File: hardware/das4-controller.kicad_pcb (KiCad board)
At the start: 4 copper layers, 51.1 x 94 mm, 76 parts, among them J1 USB-C, J2 USB-A 1, J3 USB-A 2, J4 Key matrix, SW1 Button 1, SW2 Button 2, SW3 Button 3, SW4 Button 4, SW5 Button 5, SW6 BOOTSEL, SW7 RESET, U1 RP2350B, U2 CH334R, U3 W25Q128JVS, U4 AMS1117-3.3, Y1 12MHz, Y2 12MHz

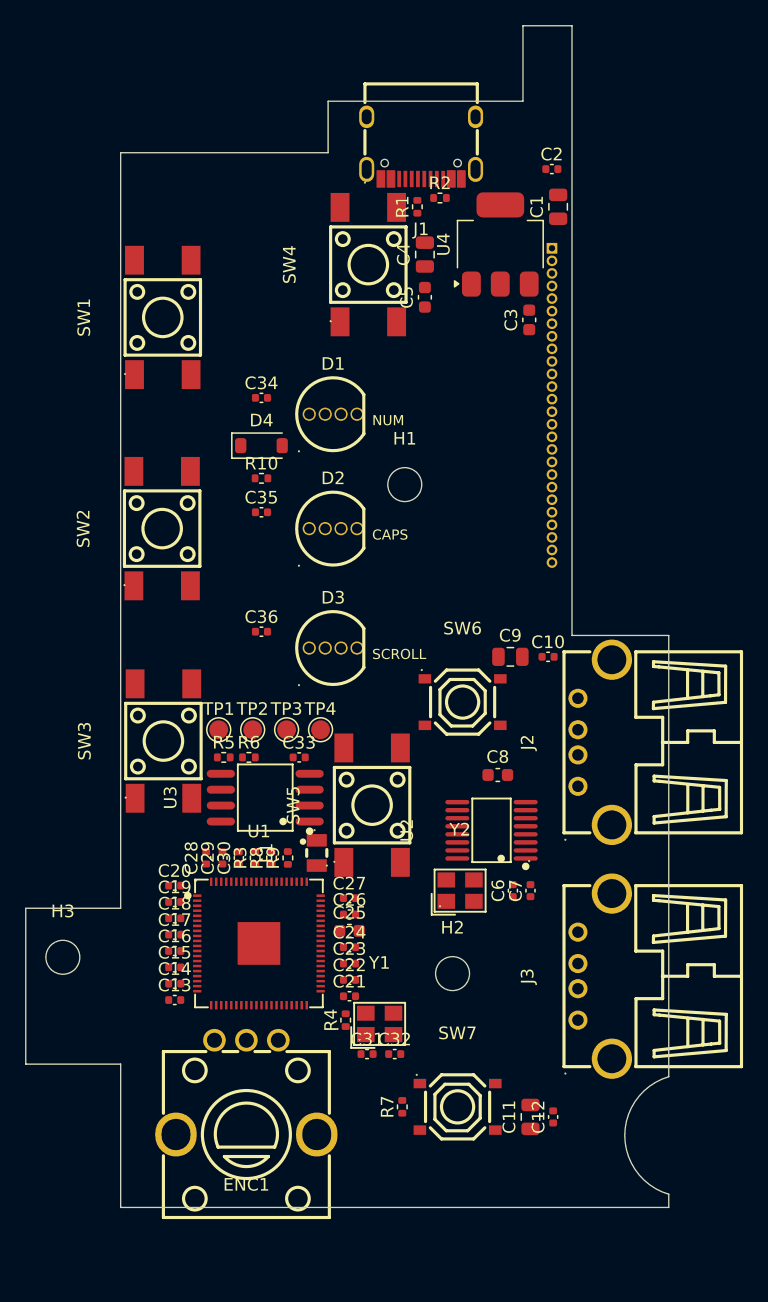
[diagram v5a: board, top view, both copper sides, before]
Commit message: Route the board: 0 unconnected, 0 real DRC violations
Circuit (from the design review):
- inductor L1 polarity per RPi (dot to +1V1); ME6211 back instead of
  AMS1117 (VBUS-sag brown-out); 2N7002 + 1k pull-up level shifter for the
  WS2812 chain (inverted data); second 4.7 uF on +1V1; RUN test pad
- J4 pin k -> GPIO(40-k): follows the package pin order so the 26-line
  bus fans out without crossings, and stays off non-5V-tolerant GPIO40-47
- USB-C: only the A4/B9 VBUS pair wired (B4/A9 is boxed in by SW4; plugs
  tie all VBUS contacts together)

Routing (make route): 4-layer F.Cu / In1 GND plane / In2 signals + 3V3
pour / B.Cu signals + GND pour. Freerouting runs 4 variants in parallel
and keeps the best. Locked pre-routes: a GND via per MCU decoupling cap,
VREG_PGND to the exposed pad, LED 5 V on In2, tact-switch pad pairs.
Afterwards ~330 GND stitching vias and vias into any via-less pour piece.

Also: net classes at JLCPCB 4-layer limits (0.1 mm), design review
write-up in docs/review-2026-09-25.md, CI checks the committed routed
board and builds the JLCPCB files, docs/fab no longer regenerate the
board.

Co-Authored-By: Claude Opus 5.5 <noreply@anthropic.com>
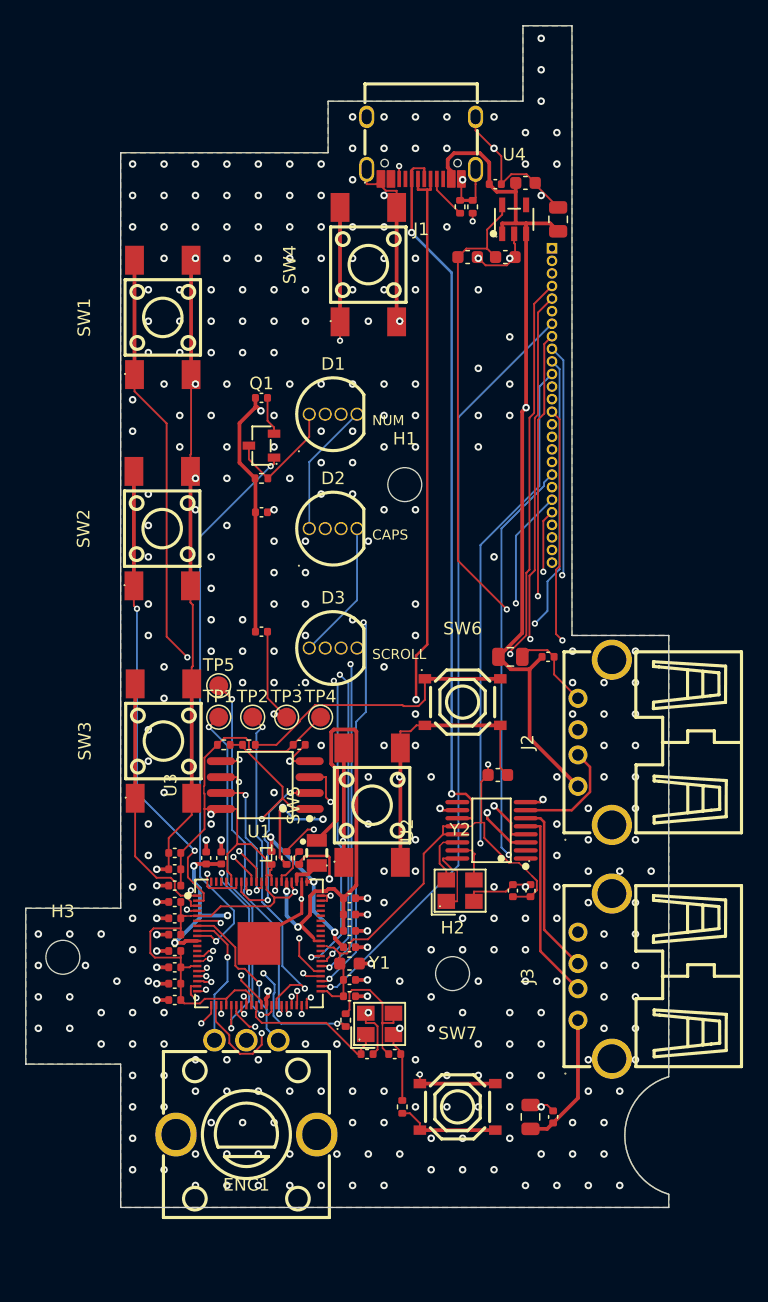
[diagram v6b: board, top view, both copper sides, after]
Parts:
- removed D4: 1N4148W, D_SOD-123
- added C37: 100n, C_0402_1005Metric, F.Cu at (111.2, 104.2)
- added Q1: 2N7002, SOT-23-3_L2.9-W1.3-P1.90-LS2.4-BR, F.Cu at (111.2, 89.4)
- added TP5: TestPoint, TestPoint_Pad_D1.5mm, F.Cu at (107.8, 108.5)
- C31: value 15p -> 4.7u
- C33: value 100n -> 15p
- C4: value 22u -> 10u; footprint C_0805_2012Metric -> C_0603_1608Metric
- R10: value 33 -> 1k
- U4: value AMS1117-3.3 -> ME6211C33M5G-N; footprint SOT-223-3_TabPin2 -> SOT-23-5_L3.0-W1.7-P0.95-LS2.8-BL
- moved C34 27.8 mm to (114.2, 113.2)
- moved C33 24.8 mm to (121.8, 137.8)
- moved C31 19.4 mm to (108.0, 122.2), turned to 90 degrees
- moved C22 17.2 mm to (104.3, 121.8), turned to 180 degrees
- moved C21 17.2 mm to (104.3, 123.1), turned to 180 degrees
- moved C28 12.3 mm to (118.2, 126.7), turned to 0 degrees
- moved C3 10.9 mm to (132.2, 68.5), turned to 0 degrees
- moved C29 10.6 mm to (118.2, 125.4), turned to 0 degrees
- moved C36 9.50 mm to (111.2, 94.7)
- moved C35 9.10 mm to (111.2, 85.6)
- moved C4 6.40 mm to (130.6, 74.4), turned to 0 degrees
- moved C5 4.67 mm to (127.6, 74.4), turned to 0 degrees
- moved C2 4.66 mm to (129.8, 68.6)
- moved R1 3.40 mm to (127.0, 70.4)
- moved R2 2.69 mm to (128.0, 70.4), turned to 90 degrees
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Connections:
- C31 pad 1: XIN -> +1V1
- C32 pad 1: XOUT_XTAL -> XIN
- C33 pad 1: +3V3 -> XOUT_XTAL
- C34 pad 1: LED1_VDD -> +3V3
- D1 pad 2: LED1_VDD -> +5V
- J1 pad B4A9: +5V -> (no net)
- L1 pad 1: +1V1 -> VREG_LX
- L1 pad 2: VREG_LX -> +1V1
- R10 pad 1: N$10 -> +5V
- U1 pad 13: (no net) -> KM26
- U1 pad 14: (no net) -> KM25
- U1 pad 16: (no net) -> KM24
- U1 pad 17: (no net) -> KM23
- U1 pad 18: (no net) -> KM22
- U1 pad 19: (no net) -> KM21
- U1 pad 20: (no net) -> KM20
- U1 pad 21: KM1 -> KM19
- U1 pad 22: KM2 -> KM18
- U1 pad 23: KM3 -> KM17
- U1 pad 25: KM4 -> KM16
- U1 pad 26: KM5 -> KM15
- U1 pad 27: KM6 -> KM14
- U1 pad 28: KM7 -> KM13
- U1 pad 36: KM8 -> KM12
- U1 pad 37: KM9 -> KM11
- U1 pad 39: KM11 -> KM9
- U1 pad 40: KM12 -> KM8
- U1 pad 42: KM13 -> KM7
- U1 pad 43: KM14 -> KM6
- U1 pad 44: KM15 -> KM5
- U1 pad 45: KM16 -> KM4
- U1 pad 46: KM17 -> KM3
- U1 pad 47: KM18 -> KM2
- U1 pad 48: KM19 -> KM1
- U1 pad 49: KM20 -> (no net)
- U1 pad 52: KM21 -> (no net)
- U1 pad 53: KM22 -> (no net)
- U1 pad 54: KM23 -> (no net)
- U1 pad 55: KM24 -> (no net)
- U1 pad 56: KM25 -> (no net)
- U1 pad 57: KM26 -> (no net)
- U1 pad 9: N$10 -> LED_DATA_N
- U4 pad 1: GND -> +5V
- U4 pad 2: +3V3 -> GND
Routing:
- net +3V3: track 0.00 -> 189.7 mm, vias 0 -> 5
- net GND: track 0.00 -> 176.7 mm, vias 0 -> 333
- net +5V: track 0.00 -> 160.2 mm, vias 0 -> 2
- net KM14: track 0.00 -> 83.4 mm, vias 0 -> 2
- net KM1: track 0.00 -> 79.1 mm, vias 0 -> 2
- net KM3: track 0.00 -> 79.0 mm, vias 0 -> 2
- net KM2: track 0.00 -> 78.3 mm, vias 0 -> 2
- net KM19: track 0.00 -> 75.7 mm, vias 0 -> 2
- net KM15: track 0.00 -> 72.2 mm, vias 0 -> 1
- net KM13: track 0.00 -> 70.4 mm, vias 0 -> 1
- net KM4: track 0.00 -> 67.5 mm, vias 0 -> 2
- net KM5: track 0.00 -> 67.1 mm, vias 0 -> 2
- net KM18: track 0.00 -> 67.0 mm, vias 0 -> 1
- net +1V1: track 0.00 -> 66.0 mm, vias 0 -> 6
- net KM9: track 0.00 -> 64.5 mm, vias 0 -> 2
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- added copper zone on In2.Cu, net +3V3
- added copper zone on B.Cu, net GND
- added copper zone on F.Cu, net GND
- added copper zone on In1.Cu, net GND

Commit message: Re-layout the MCU corner per the layout review, re-route
U1 rotated 90 degrees; the critical nets are now drawn by hand in
hardware/scripts/critical.py and locked before autorouting, following
Raspberry Pi's minimal-design layout:
- core regulator block at pins 61-65 (VREG_VIN/+1V1 caps at the pins, LX
  between their pads into L1, GND vias, VREG_AVDD RC filter)
- 3x3 via array in the exposed GND pad
- inward vias from every +3V3 pin (In2 is now a solid +3V3 plane) and
  +1V1 pin (0.5 mm +1V1 "C" spine on B.Cu)
- decap columns with shared GND vias, crystal beside XIN/XOUT
- USB upstream as a coupled pair over solid GND, clear of H1; CC resistors

route.py: every other +3V3/GND SMD pad gets its own via into its plane
before autorouting; signal vias the router didn't use are removed after.
Buttons moved to GPIO42-47, LED data to GPIO44.

Result: 0 unconnected, 0 non-cosmetic DRC violations.

Co-Authored-By: Claude Opus 5.5 <noreply@anthropic.com>
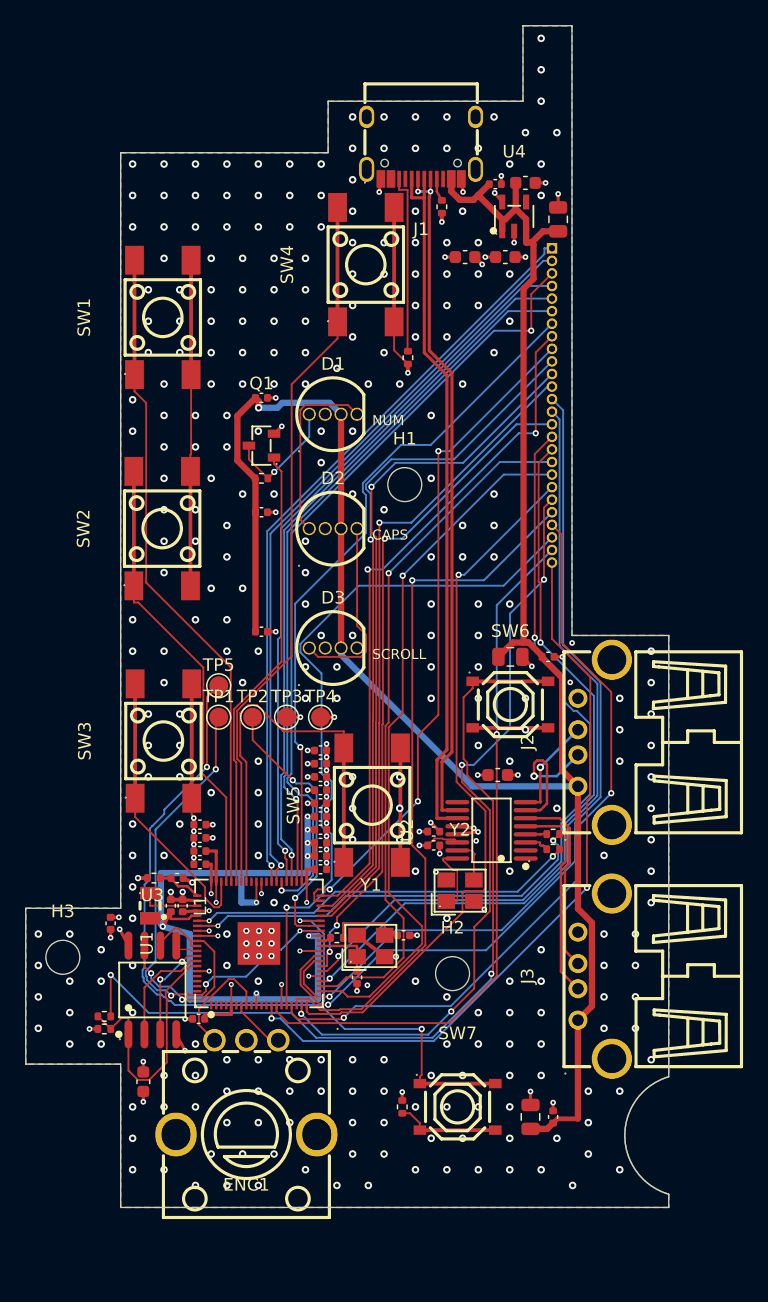
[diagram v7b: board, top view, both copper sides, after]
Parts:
- removed C13, C14, C15, C16, C17, C18, C19, C20, C21, C22, C23, C27, C28, C29, C34: 100n, C_0402_1005Metric
- removed C24, C26, C30, C31: 4.7u, C_0402_1005Metric
- removed C25: 10u, C_0603_1608Metric
- removed C32, C33: 15p, C_0402_1005Metric
- removed R3: 33, R_0402_1005Metric
- removed R4, R6, R7: 1k, R_0402_1005Metric
- removed R5: 10k, R_0402_1005Metric
- removed R8, R9: 22, R_0402_1005Metric
- added C105: 100n, C_0402_1005Metric, F.Cu at (106.2, 135.0)
- added C110: 100n, C_0402_1005Metric, F.Cu at (115.9, 120.0)
- added C115: 100n, C_0402_1005Metric, F.Cu at (115.9, 113.7)
- added C124: 100n, C_0402_1005Metric, F.Cu at (115.9, 116.8)
- added C129: 100n, C_0402_1005Metric, F.Cu at (115.9, 115.8)
- added C132: 100n, C_0402_1005Metric, F.Cu at (115.9, 121.0)
- added C141: 100n, C_0402_1005Metric, F.Cu at (115.9, 123.1)
- added C150: 100n, C_0402_1005Metric, F.Cu at (115.9, 117.8)
- added C151: 100n, C_0402_1005Metric, F.Cu at (115.9, 122.0)
- added C159: 100n, C_0402_1005Metric, F.Cu at (106.3, 121.7)
- added C160: 100n, C_0402_1005Metric, F.Cu at (106.3, 122.7)
- added C161: 4.7u, C_0402_1005Metric, F.Cu at (104.5, 123.8)
- added C164: 4.7u, C_0402_1005Metric, F.Cu at (104.9, 126.0)
- added C165: 4.7u, C_0402_1005Metric, F.Cu at (104.0, 126.0)
- added C166: 4.7u, C_0402_1005Metric, F.Cu at (115.9, 118.9)
- added C168: 100n, C_0402_1005Metric, F.Cu at (106.3, 119.5)
- added C169: 100n, C_0402_1005Metric, F.Cu at (115.9, 114.7)
- added C176: 100n, C_0402_1005Metric, F.Cu at (106.3, 120.6)
- added C190: 10u, C_0603_1608Metric, F.Cu at (101.8, 140.0)
- added C230: 15p, C_0402_1005Metric, F.Cu at (118.8, 131.7)
- added C231: 15p, C_0402_1005Metric, F.Cu at (122.5, 128.3)
- added C300: 100n, C_0402_1005Metric, F.Cu at (99.2, 127.4)
- added R161: 33, R_0402_1005Metric, F.Cu at (102.6, 123.8)
- added R231: 1k, R_0402_1005Metric, F.Cu at (117.2, 128.6)
- added R266: 22, R_0402_1005Metric, F.Cu at (134.4, 121.5)
- added R267: 22, R_0402_1005Metric, F.Cu at (134.4, 120.3)
- added R301: 10k, R_0402_1005Metric, F.Cu at (98.7, 135.8)
- added R302: 1k, R_0402_1005Metric, F.Cu at (98.7, 134.8)
- added R303: 1k, R_0402_1005Metric, F.Cu at (122.4, 142.0)
- moved U3 18.6 mm to (102.5, 132.7), turned to 0 degrees
- moved L1 13.9 mm to (102.3, 126.0), turned to -90 degrees
- moved R2 13.1 mm to (122.8, 82.4), turned to -90 degrees
- moved C7 9.02 mm to (124.9, 120.1), turned to 180 degrees
- moved C6 7.26 mm to (124.9, 121.2), turned to 180 degrees
- moved Y1 6.24 mm to (119.9, 129.2)
- moved SW6 3.81 mm to (131.0, 110.0)
- moved R1 1.45 mm to (125.5, 70.4), turned to -90 degrees
- moved U4 0.23 mm to (131.3, 71.2)
- moved SW4 0.20 mm to (119.5, 75.0)
- moved C5 0.20 mm to (127.4, 74.4)
- turned U1 to 90 degrees
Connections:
- U1 pad 1: BTN1 -> (no net)
- U1 pad 2: BTN2 -> (no net)
- U1 pad 3: BTN3 -> (no net)
- U1 pad 4: BTN4 -> (no net)
- U1 pad 53: (no net) -> BTN5
- U1 pad 54: (no net) -> BTN4
- U1 pad 55: (no net) -> LED_DATA_N
- U1 pad 56: (no net) -> BTN1
- U1 pad 57: (no net) -> BTN2
- U1 pad 58: (no net) -> BTN3
- U1 pad 6: BTN5 -> (no net)
- U1 pad 9: LED_DATA_N -> (no net)
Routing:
- net +3V3: track 189.7 -> 44.0 mm, vias 5 -> 33
- net GND: track 176.7 -> 120.4 mm, vias 333 -> 362
- net USB_BOOT: track 22.8 -> 68.6 mm, vias 0 -> 2
- net N$7: track 3.16 -> 31.2 mm, vias 0 -> 2
- net USB_MCU_D+: track 26.5 -> 1.68 mm, vias 3 -> 0
- net N$6: track 9.83 -> 33.3 mm
- net USB_MCU_D-: track 23.6 -> 2.01 mm, vias 2 -> 0
- net RUN: track 49.0 -> 69.9 mm
- net KM19: track 75.7 -> 56.1 mm, vias 2 -> 1
- net KM1: track 79.1 -> 60.3 mm, vias 2 -> 1
- net KM15: track 72.2 -> 53.5 mm, vias 1 -> 3
- net KM2: track 78.3 -> 59.6 mm, vias 2 -> 1
- net KM14: track 83.4 -> 66.9 mm, vias 2 -> 1
- net KM3: track 79.0 -> 63.2 mm
- net KM26: track 44.2 -> 59.2 mm, vias 1 -> 2
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
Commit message: Fix layout review 2: keep-outs, DVDD cap, EP paste, re-route
- Rule areas: no copper on In1/In2/B.Cu under L1 and VREG_LX (RP2350
  datasheet 6.3.8); no F.Cu pour round the regulator block (GND at one
  point); no F.Cu tracks/vias under the USB-A shells; 2.5 mm clear round
  the mounting holes; router-only keep-out round the crystal block
- +1V1 spine leaves under U1's left pad row (clear of L1/LX and the QSPI
  flash gap)
- C110 right under DVDD pin 10; encoder moved to GPIO13 (A) / GPIO8 (B)
- EP: 5 vias in a "+" with 4 paste windows between them (~50 %)
- decap columns at 1.2 mm pitch so shared GND vias clear the pads; plane
  fanout vias never touch their own pad
- LX enters L1 from outside its body; LED +5V hand-routed
- docs/review-layout-2-2026-09-25.md: the review, plus what was done

0 unconnected, 0 non-cosmetic DRC violations in all 4 router variants.
J4 is still a placeholder.

Co-Authored-By: Claude Opus 5.5 <noreply@anthropic.com>
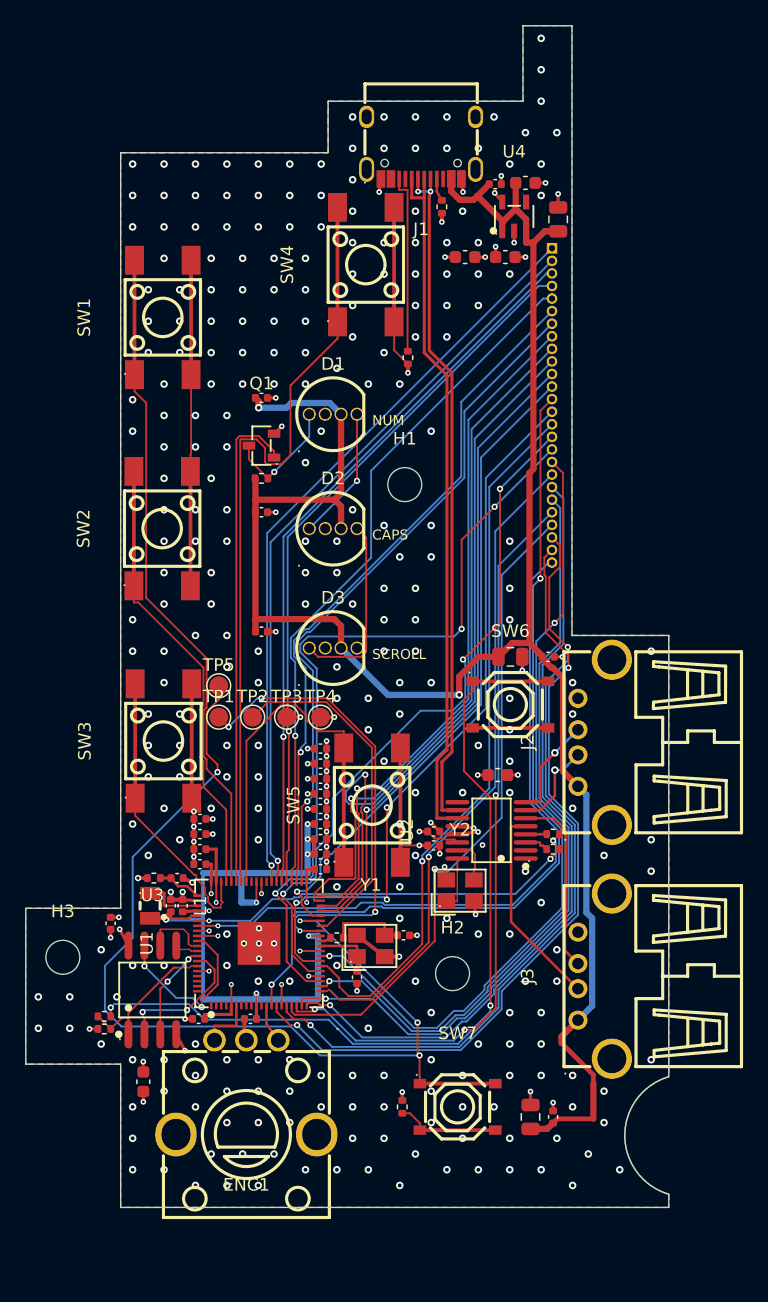
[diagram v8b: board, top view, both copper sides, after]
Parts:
- moved C110 16.1 mm to (110.3, 135.0), turned to 180 degrees
- moved C166 0.60 mm to (115.9, 119.5)
- moved C150 0.45 mm to (115.9, 118.3)
- moved C168 0.45 mm to (106.3, 119.1)
- moved C124 0.30 mm to (115.9, 117.1)
- moved C132 0.30 mm to (115.9, 120.7)
- moved C176 0.30 mm to (106.3, 120.3)
- moved C115 0.15 mm to (115.9, 113.5)
- moved C129 0.15 mm to (115.9, 115.9)
- moved C159 0.15 mm to (106.3, 121.5)
- moved C151 0.15 mm to (115.9, 121.9)
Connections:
- U1 pad 12: (no net) -> ENC_A
- U1 pad 6: (no net) -> ENC_B
- U1 pad 7: ENC_A -> (no net)
- U1 pad 8: ENC_B -> (no net)
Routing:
- net RUN: track 69.9 -> 82.1 mm, vias 3 -> 4
- net KM14: track 66.9 -> 58.1 mm, vias 1 -> 3
- net QSPI_SS: track 20.3 -> 11.9 mm
- net KM18: track 55.5 -> 63.4 mm, vias 1 -> 2
- net KM23: track 59.5 -> 52.3 mm, vias 2 -> 1
- net KM25: track 55.7 -> 62.7 mm, vias 1 -> 2
- net +5V: track 167.6 -> 161.1 mm, vias 1 -> 2
- net KM20: track 56.1 -> 62.4 mm
- net KM24: track 56.8 -> 62.7 mm, vias 1 -> 2
- net N$9: track 22.0 -> 27.7 mm, vias 2 -> 0
- net KM3: track 63.2 -> 57.5 mm, vias 2 -> 1
- net GND: track 120.4 -> 125.8 mm, vias 362 -> 334
- net BTN4: track 57.1 -> 62.2 mm
- net ENC_B: track 9.26 -> 4.53 mm
- net +1V1: track 61.7 -> 57.0 mm, vias 8 -> 7
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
